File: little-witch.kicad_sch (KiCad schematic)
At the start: 34 parts, among them J1 GCT-USB4105, J3 Conn_ARM_SWD_TagConnect_TC203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, J4 GCT-USB4105, J5 Conn_02x20_Odd_Even, SW1 RESET, SW2 BOOT0, SW3 SW_SPST, U1 CH32V307RCT6, Y1 SIT8008BI-73-33N-25.000000

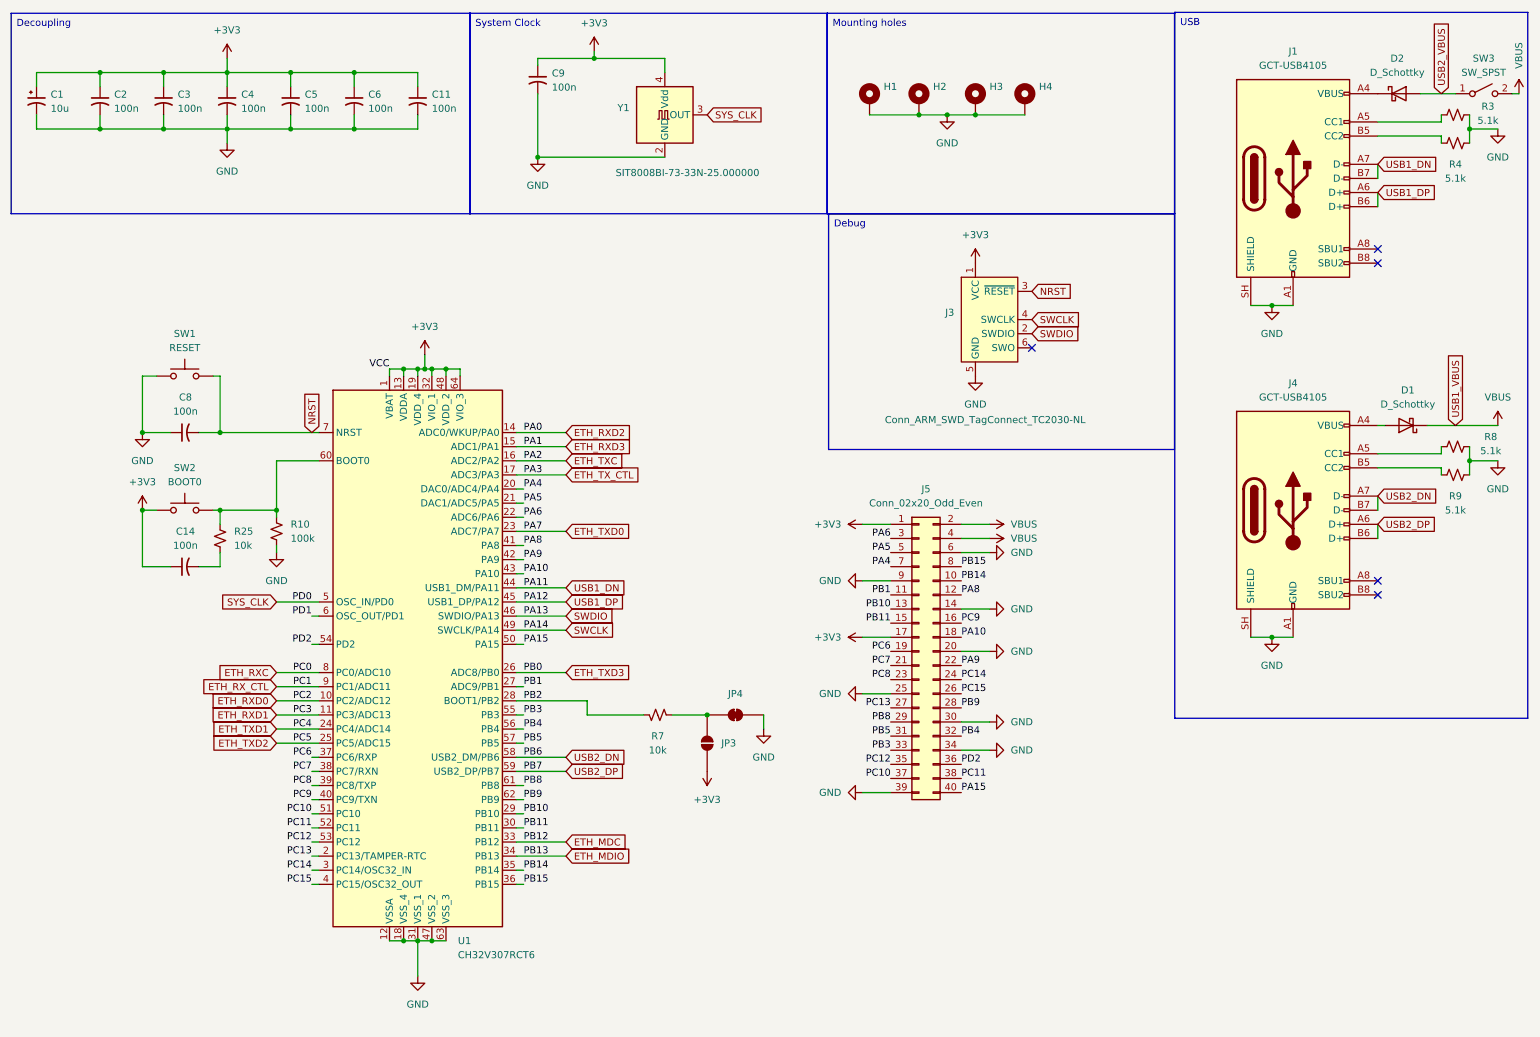
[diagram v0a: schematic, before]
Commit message: Start of changes for v0.3
- Drop USB FS for unpopulated header
- Add LEDs
- Tweak BOOT0 debouncing
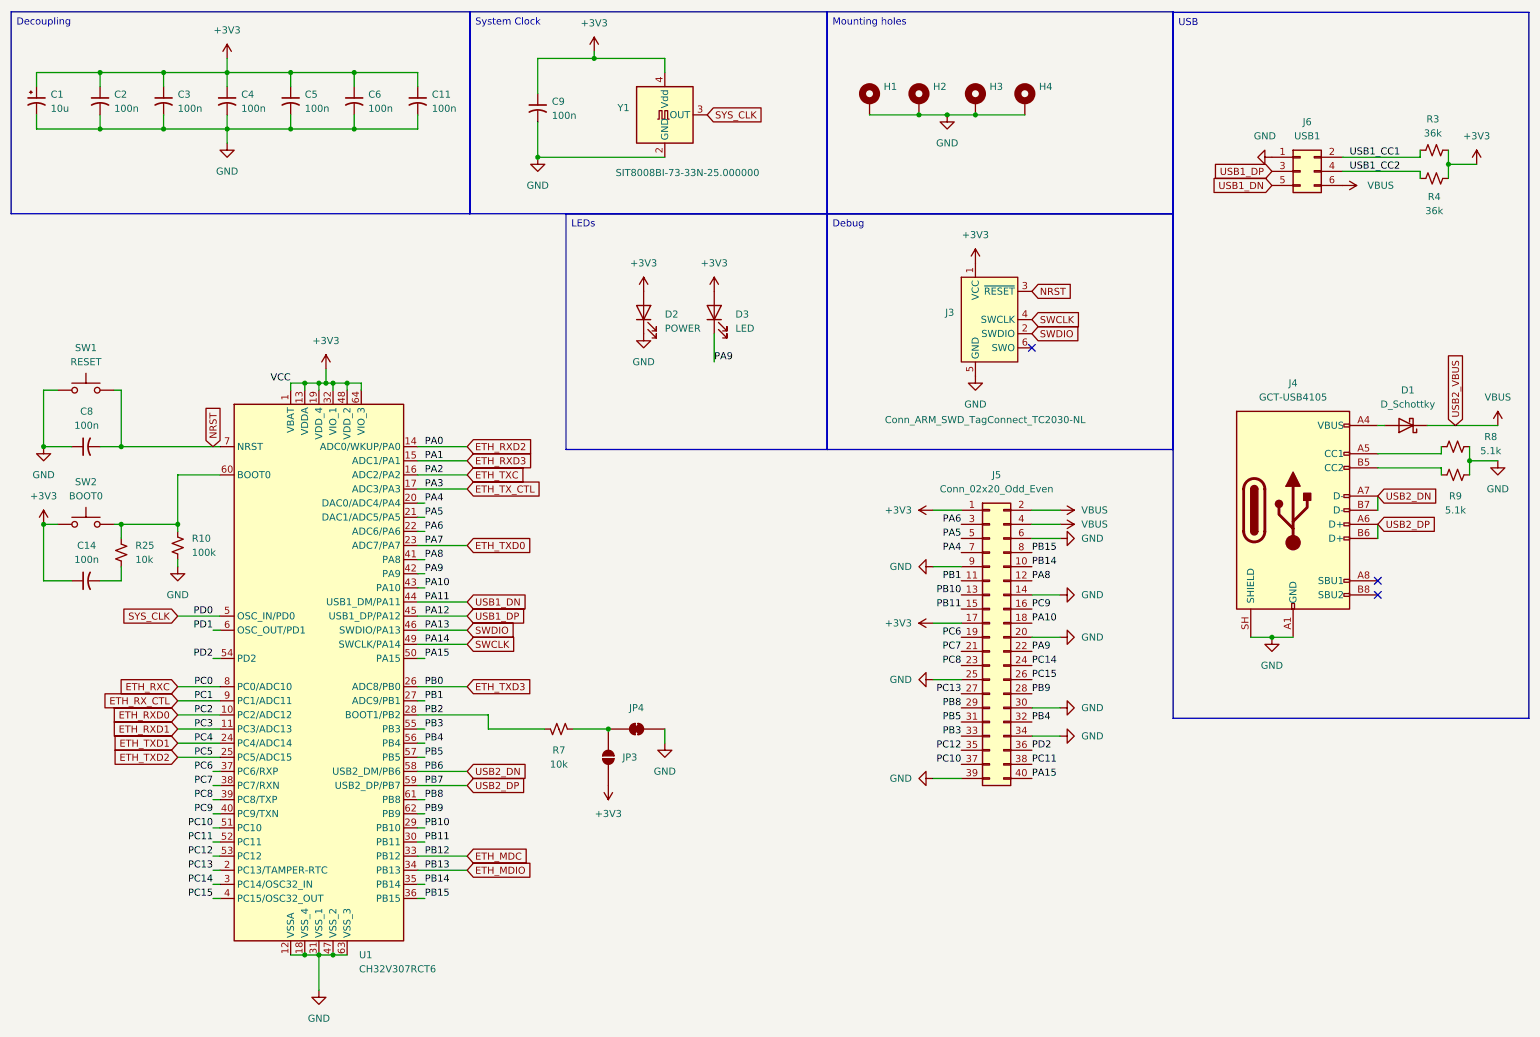
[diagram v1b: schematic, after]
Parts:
- removed D2: D_Schottky, symbol Device:D_Schottky
- removed J1: GCT-USB4105, Connector_USB:USB_C_Receptacle_GCT_USB4105-xx-A_16P_TopMnt_Horizontal, symbol Connector:USB_C_Receptacle_USB2.0_16P
- removed SW3: SW_SPST, symbol Switch:SW_SPST
- added D2: POWER, symbol Device:LED
- added D3: LED, symbol Device:LED
- added J6: USB1, Connector_PinSocket_2.54mm:PinSocket_2x03_P2.54mm_Vertical, symbol Connector_Generic:Conn_02x03_Odd_Even
- R3, R4: value 5.1k -> 36k
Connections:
- net +3V3: now also R3.2, R4.1, D2.2 (A), D3.2 (A)
- net GND: now also D2.1 (K), J6.1 (Pin_1); no longer R3.2, R4.1
- net PA9: now also D3.1 (K)
- net USB1_DN: now also J6.5 (Pin_5)
- net USB1_DP: now also J6.3 (Pin_3)
- net VBUS: now also J6.6 (Pin_6)
- net USB1_CC2: now reaches R4.2
- net USB1_CC2: now also J6.4 (Pin_4)
- net USB1_CC1: now reaches R3.1
- net USB1_CC1: now also J6.2 (Pin_2)
- no-connect marks 5 -> 3
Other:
- moved on the sheet: C14, C8, C9, J5, JP3, JP4, R10, R25, R7, SW1, SW2, U1

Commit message: Continued pin choice work
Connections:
- net ETH_MDC: now also J5.12 (Pin_12)
- net ETH_MDIO: now also J5.40 (Pin_40)
- net PA10: now also J5.10 (Pin_10); no longer J5.18 (Pin_18)
- net PA15: now also J5.24 (Pin_24); no longer J5.40 (Pin_40)
- net PA4: no longer J5.7 (Pin_7)
- net PA5: no longer J5.5 (Pin_5)
- net PA6: no longer J5.3 (Pin_3)
- net PA8: no longer J5.12 (Pin_12)
- net PA9: now also J5.8 (Pin_8); no longer J5.22 (Pin_22)
- net PB1: no longer J5.11 (Pin_11)
- net PB10: now also J5.5 (Pin_5); no longer J5.13 (Pin_13)
- net PB11: now also J5.3 (Pin_3); no longer J5.15 (Pin_15)
- net PB14: now also J5.35 (Pin_35); no longer J5.10 (Pin_10)
- net PB15: now also J5.38 (Pin_38); no longer J5.8 (Pin_8)
- net PB3: now also J5.23 (Pin_23); no longer J5.33 (Pin_33)
- net PB4: now also J5.21 (Pin_21); no longer J5.32 (Pin_32)
- net PB5: now also J5.19 (Pin_19); no longer J5.31 (Pin_31)
- net PB8: now also J5.28 (Pin_28); no longer J5.29 (Pin_29)
- net PB9: now also J5.27 (Pin_27); no longer J5.28 (Pin_28)
- net PC11: now also J5.13 (Pin_13); no longer J5.38 (Pin_38)
- net PC12: now also J5.15 (Pin_15); no longer J5.35 (Pin_35)
- net PC13: no longer J5.27 (Pin_27)
- net PC14: no longer J5.24 (Pin_24)
- net PC15: no longer J5.26 (Pin_26)
- net PC6: no longer J5.19 (Pin_19)
- net PC7: no longer J5.21 (Pin_21)
- net PC8: now also J5.18 (Pin_18); no longer J5.23 (Pin_23)
- net PC9: now also J5.22 (Pin_22); no longer J5.16 (Pin_16)
- net PD2: now also J5.16 (Pin_16); no longer J5.36 (Pin_36)

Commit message: More pin assignments
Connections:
- net PB1: now also J5.7 (Pin_7)
- net PC13: now also J5.29 (Pin_29)
- net PC14: now also J5.31 (Pin_31)
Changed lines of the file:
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@@
 	)
 	(label "PB1"
-		(at 165.1 114.3 180)
+		(at 182.88 109.22 180)
 		(effects
 			(font
@@
 	)
 	(label "PC13"
-		(at 165.1 134.62 180)
+		(at 182.88 137.16 180)
 		(effects
 			(font
@@
 	)
 	(label "PC14"
-		(at 212.09 130.81 0)
+		(at 182.88 139.7 180)
 		(effects
 			(font
 				(size 1.27 1.27)
 			)
-			(justify left bottom)
+			(justify right bottom)
 		)
 	)

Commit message: Finish pin assignment
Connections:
- net PA4: now also J5.11 (Pin_11)
- net PA5: now also J5.26 (Pin_26)
- net PA6: now also J5.36 (Pin_36)
- net PC15: now also J5.32 (Pin_32)
- net PC7: now also J5.33 (Pin_33)
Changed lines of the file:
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@@
 	)
 	(label "PA5"
-		(at 165.1 106.68 180)
-		(effects
-			(font
-				(size 1.27 1.27)
-			)
-			(justify right bottom)
+		(at 195.58 132.08 0)
+		(effects
+			(font
+				(size 1.27 1.27)
+			)
+			(justify left bottom)
 		)
 	)
@@
 	)
 	(label "PA4"
-		(at 165.1 109.22 180)
+		(at 182.88 114.3 180)
 		(effects
 			(font
@@
 	)
 	(label "PA6"
-		(at 165.1 104.14 180)
-		(effects
-			(font
-				(size 1.27 1.27)
-			)
-			(justify right bottom)
+		(at 195.58 144.78 0)
+		(effects
+			(font
+				(size 1.27 1.27)
+			)
+			(justify left bottom)
 		)
 	)
 	(label "PC7"
-		(at 165.1 127 180)
+		(at 182.88 142.24 180)
 		(effects
 			(font
@@
 		)
 	)
-	(label "PC6"
-		(at 165.1 124.46 180)
-		(effects
-			(font
-				(size 1.27 1.27)
-			)
-			(justify right bottom)
-		)
-	)
 	(label "PA6"
 		(at 86.36 105.41 0)
@@
 		)
 	)
-	(label "PA8"
-		(at 212.09 115.57 0)
-		(effects
-			(font
-				(size 1.27 1.27)
-			)
-			(justify left bottom)
-		)
-	)
 	(label "PB5"
 		(at 86.36 146.05 0)
@@
 	)
 	(label "PC15"
-		(at 212.09 133.35 0)
-		(effects
-			(font
+		(at 195.58 139.7 0)
+		(effects
+			(font

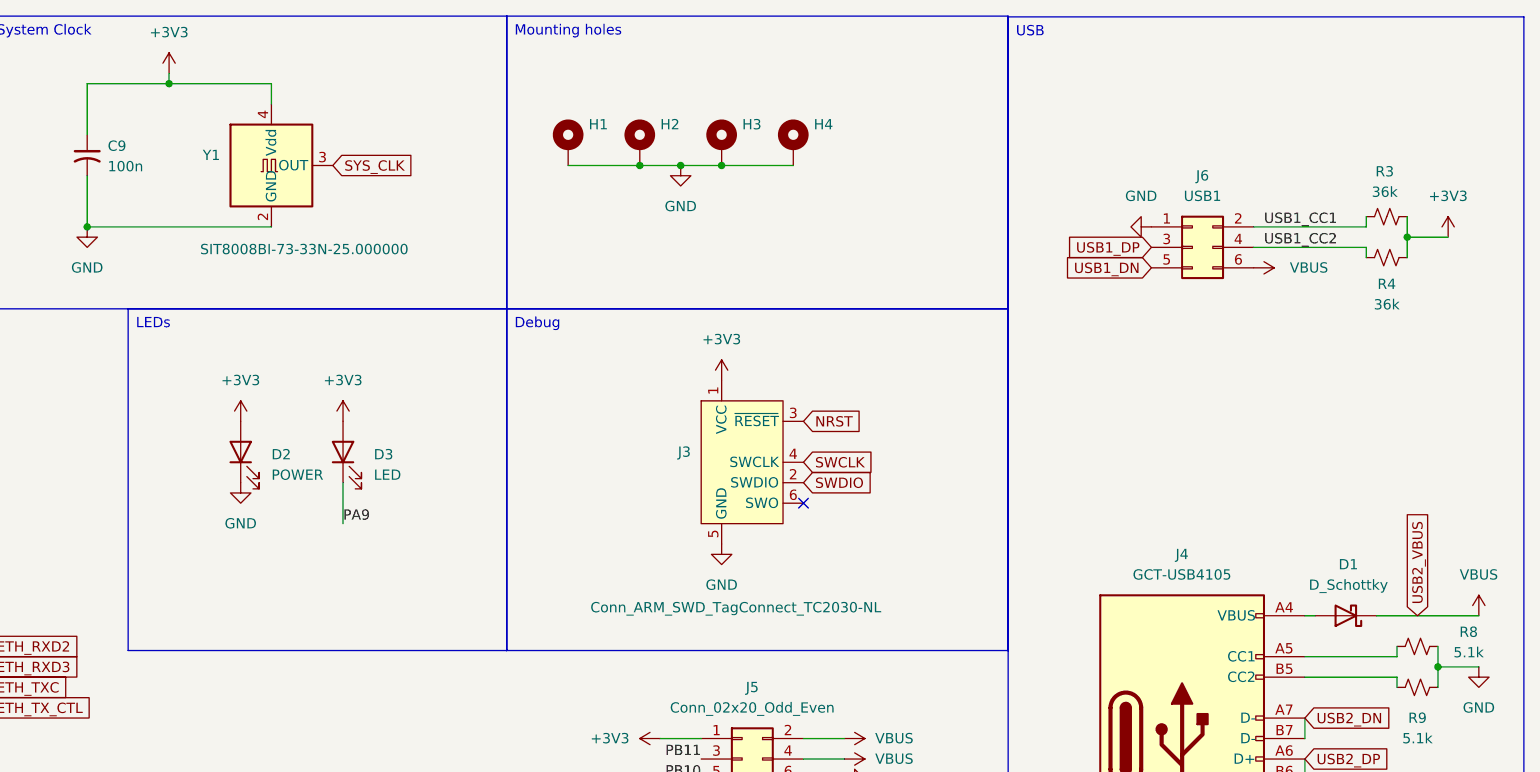
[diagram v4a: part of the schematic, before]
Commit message: Power/LED tweaks, GPIO routing
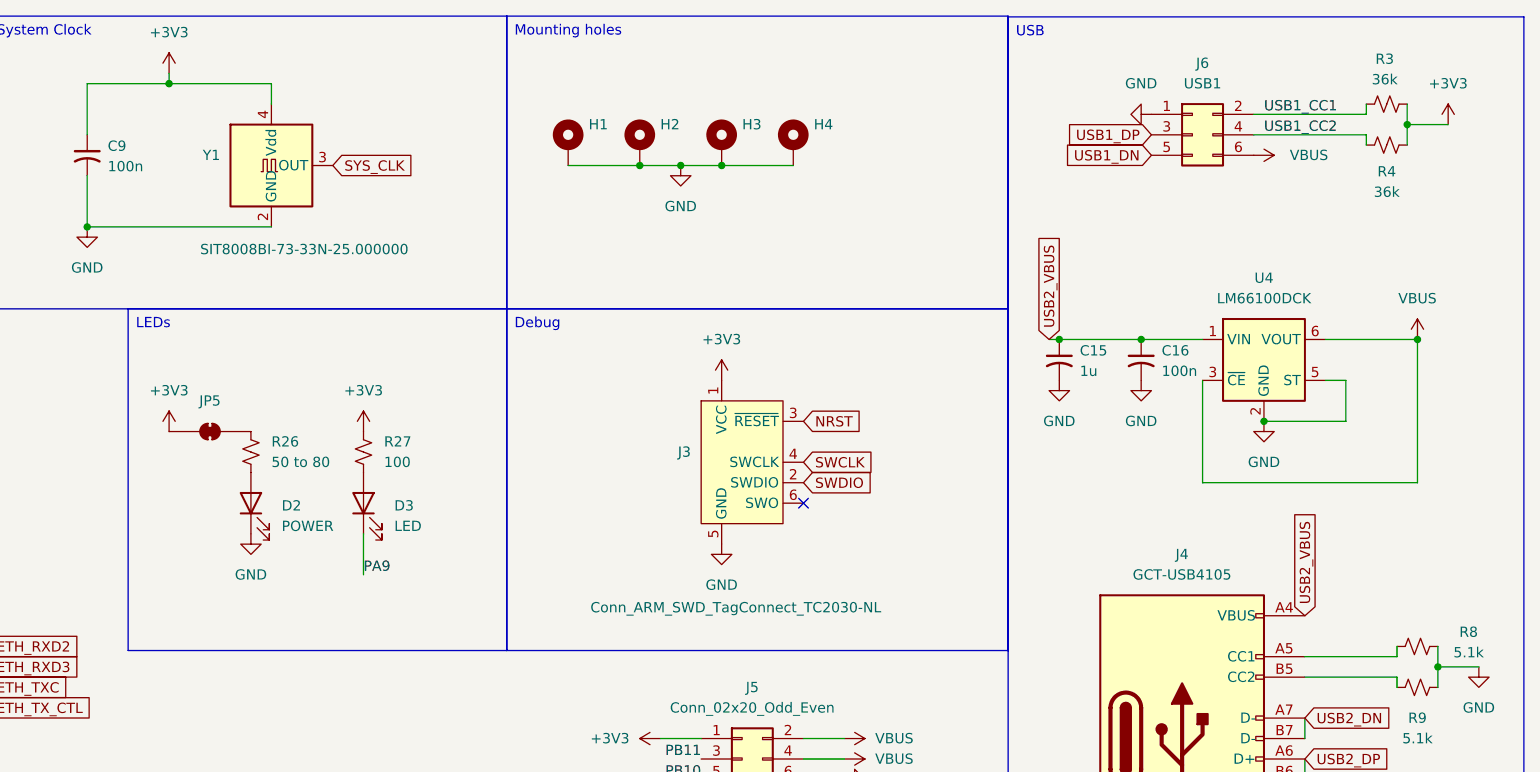
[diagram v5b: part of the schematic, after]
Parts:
- removed D1: D_Schottky, symbol Device:D_Schottky
- added C15: 1u, Capacitor_SMD:C_0402_1005Metric, symbol Device:C_Small_US
- added C16: 100n, Capacitor_SMD:C_0402_1005Metric, symbol Device:C_Small_US
- added JP5: SolderJumper_2_Open, Jumper:SolderJumper-2_P1.3mm_Bridged_RoundedPad1.0x1.5mm, symbol Jumper:SolderJumper_2_Bridged
- added R26: 50 to 80, Resistor_SMD:R_0402_1005Metric, symbol Device:R_Small_US
- added R27: 100, Resistor_SMD:R_0402_1005Metric, symbol Device:R_Small_US
- added U4: LM66100DCK, Package_TO_SOT_SMD:SOT-363_SC-70-6, symbol Power_Management:LM66100DCK
- D2, D3: footprint (none) -> LED_SMD:LED_0603_1608Metric
- J6: footprint Connector_PinSocket_2.54mm:PinSocket_2x03_P2.54mm_Vertical -> Connector_PinSocket_1.27mm:PinSocket_2x03_P1.27mm_Vertical; now left out of the parts list
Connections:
- net +3V3: now also JP5.1 (A), R27.2; no longer D2.2 (A), D3.2 (A)
- net GND: now also C15.2, C16.2, U4.2 (GND), U4.5 (ST)
- net VBUS: now also U4.3 (~{CE}), U4.6 (VOUT)
- net USB2_VBUS: now reaches J4.A4 (VBUS), J4.A9 (VBUS), J4.B4 (VBUS), J4.B9 (VBUS)
- net USB2_VBUS: now also C15.1, C16.1, U4.1 (VIN)
- new net: D3.2 (A), R27.1
- new net: JP5.2 (B), R26.2
- new net: D2.2 (A), R26.1
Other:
- moved on the sheet: D2, D3, J6, R3, R4
